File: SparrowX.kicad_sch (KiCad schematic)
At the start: 30 parts, among them J1 NORTH, J2 SOUTH, J3 WEST, J4 EAST, U1 LMR43610MSC3RPERQ1, U2 LD49100PU33RY, U3 STM32G0B1CBU6, U4 TCAN332G, U5 TCAN332G

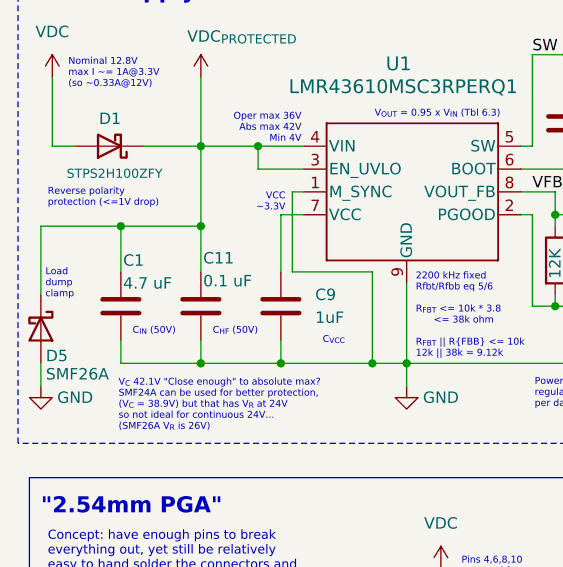
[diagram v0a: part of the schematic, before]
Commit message: DFM: get rid of 0201 SMD components
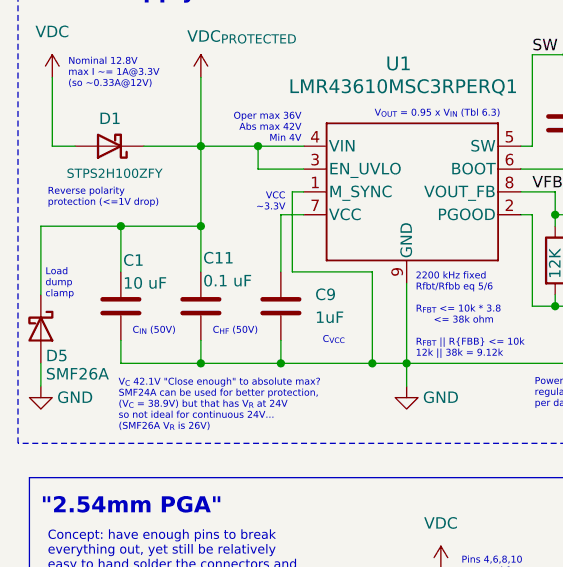
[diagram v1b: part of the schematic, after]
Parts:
- C1, C2: footprint Capacitor_SMD:C_0201_0603Metric -> Capacitor_SMD:C_0402_1005Metric
- C1: value 4.7 uF -> 10 uF
- R1: footprint Resistor_SMD:R_0201_0603Metric -> Resistor_SMD:R_0402_1005Metric
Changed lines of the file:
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@@
 			)
 		)
-		(property "Footprint" "Capacitor_SMD:C_0201_0603Metric"
+		(property "Footprint" "Capacitor_SMD:C_0402_1005Metric"
 			(at 106.68 70.8152 0)
 			(effects
@@
 			)
 		)
-		(property "Footprint" "Resistor_SMD:R_0201_0603Metric"
+		(property "Footprint" "Resistor_SMD:R_0402_1005Metric"
 			(at 98.552 85.09 90)
 			(effects
@@
 			)
 		)
-		(property "Value" "4.7 uF"
+		(property "Value" "10 uF"
 			(at 24.384 48.2599 0)
 			(effects
@@
 			)
 		)
-		(property "Footprint" "Capacitor_SMD:C_0201_0603Metric"
+		(property "Footprint" "Capacitor_SMD:C_0402_1005Metric"
 			(at 101.2952 106.68 0)
 			(effects

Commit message: A2 revision
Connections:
- net GND: now also J1.2 (Pin_2); no longer J3.1 (Pin_1)
- net SWCLK: now also J3.7 (Pin_7); no longer J3.8 (Pin_8)
- net SWDIO: now also J3.8 (Pin_8); no longer J3.7 (Pin_7)
- net VDC: no longer J1.2 (Pin_2)
- no-connect marks 11 -> 12
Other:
- note added: "PIN 1 is key pin"
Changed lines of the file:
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@@
 	)
 	(junction
-		(at 78.74 57.15)
+		(at 72.39 82.55)
 		(diameter 0)
 		(color 0 0 0 0)
 	)
 	(junction
-		(at 27.94 130.81)
+		(at 78.74 57.15)
 		(diameter 0)
 		(color 0 0 0 0)
@@
 	)
 	(no_connect
+		(at 30.48 107.95)
+	)
+	(no_connect
 		(at 74.93 97.79)
 	)
@@
 	(wire
 		(pts
-			(xy 27.94 107.95) (xy 30.48 107.95)
-		)
-		(stroke
-			(width 0)
-			(type default)
-		)
-	)
-	(wire
-		(pts
 			(xy 123.19 36.83) (xy 123.19 45.72)
 		)
@@
 	(wire
 		(pts
-			(xy 27.94 130.81) (xy 27.94 107.95)
-		)
-		(stroke
-			(width 0)
-			(type default)
-		)
-	)
-	(wire
-		(pts
 			(xy 176.53 102.87) (xy 190.5 102.87)
 		)
@@
 	(wire
 		(pts
+			(xy 59.69 82.55) (xy 72.39 82.55)
+		)
+		(stroke
+			(width 0)
+			(type default)
+		)
+	)
+	(wire
+		(pts
 			(xy 30.48 128.27) (xy 21.59 128.27)
 		)
@@
 	(wire
 		(pts
-			(xy 59.69 80.01) (xy 59.69 85.09)
-		)
-		(stroke
-			(width 0)
-			(type default)
-		)
-	)
-	(wire
-		(pts
 			(xy 176.53 87.63) (xy 190.5 87.63)
 		)
@@
 	(wire
 		(pts
+			(xy 59.69 85.09) (xy 59.69 82.55)
+		)
+		(stroke
+			(width 0)
+			(type default)
+		)
+	)
+	(wire
+		(pts
 			(xy 139.7 71.12) (xy 139.7 57.15)
 		)
@@
 		)
 	)
+	(text "PIN 1 is\nkey pin"
+		(exclude_from_sim no)
+		(at 31.242 106.426 0)
+		(effects
+			(font
+				(size 0.762 0.762)
+			)
+			(justify right bottom)
+		)
+	)
 	(text "R_{FBT}\n1%"
 		(exclude_from_sim no)
@@
 	(text "Pins 4,6,8,10\nreserved for\nfuture boards\nwith 4x CAN"
 		(exclude_from_sim no)
-		(at 61.976 83.312 0)
+		(at 61.976 81.788 0)
 		(effects
 			(font
@@
 	)
 	(label "SWDIO"
-		(at 21.59 115.57 0)
+		(at 52.07 115.57 180)
 		(fields_autoplaced yes)
 		(effects
@@
 				(size 1.27 1.27)
 			)
-			(justify left bottom)
+			(justify right bottom)
 		)
 	)
@@
 	)
 	(label "SWCLK"
-		(at 52.07 115.57 180)
+		(at 21.59 115.57 0)
 		(fields_autoplaced yes)
 		(effects
@@
 				(size 1.27 1.27)
 			)
-			(justify right bottom)
+			(justify left bottom)
 		)
 	)
@@
 					(unit 1)
 				)
-			)
-		)
-	)
-	(symbol
-		(lib_id "power:VDC")
-		(at 59.69 80.01 0)
-		(unit 1)
-		(exclude_from_sim no)
-		(in_bom yes)
-		(on_board yes)
-		(dnp no)
-		(property "Reference" "#PWR019"
-			(at 59.69 82.55 0)
-			(effects
-				(font
-					(size 1.27 1.27)
-				)
-				(hide yes)
-			)
-		)
-		(property "Value" "VDC"
-			(at 59.69 74.93 0)
-			(effects
-				(font
-					(size 1.27 1.27)
-				)
-			)
-		)
-		(property "Footprint" ""
-			(at 59.69 80.01 0)
-			(effects
-				(font
-					(size 1.27 1.27)
-				)
-				(hide yes)
-			)
-		)
-		(property "Datasheet" ""
-			(at 59.69 80.01 0)
-			(effects
-				(font
-					(size 1.27 1.27)
-				)
-				(hide yes)
-			)
-		)
-		(property "Description" ""
-			(at 59.69 80.01 0)
-			(effects
-				(font
-					(size 1.27 1.27)
-				)
-				(hide yes)
-			)
-		)
-		(pin "1"
-		)
-		(instances
-			(project "SparrowX"
-				(path "/c35a64e4-2c93-4785-901b-32ffcab28aed"
-					(reference "#PWR019")
-					(unit 1)
-				)

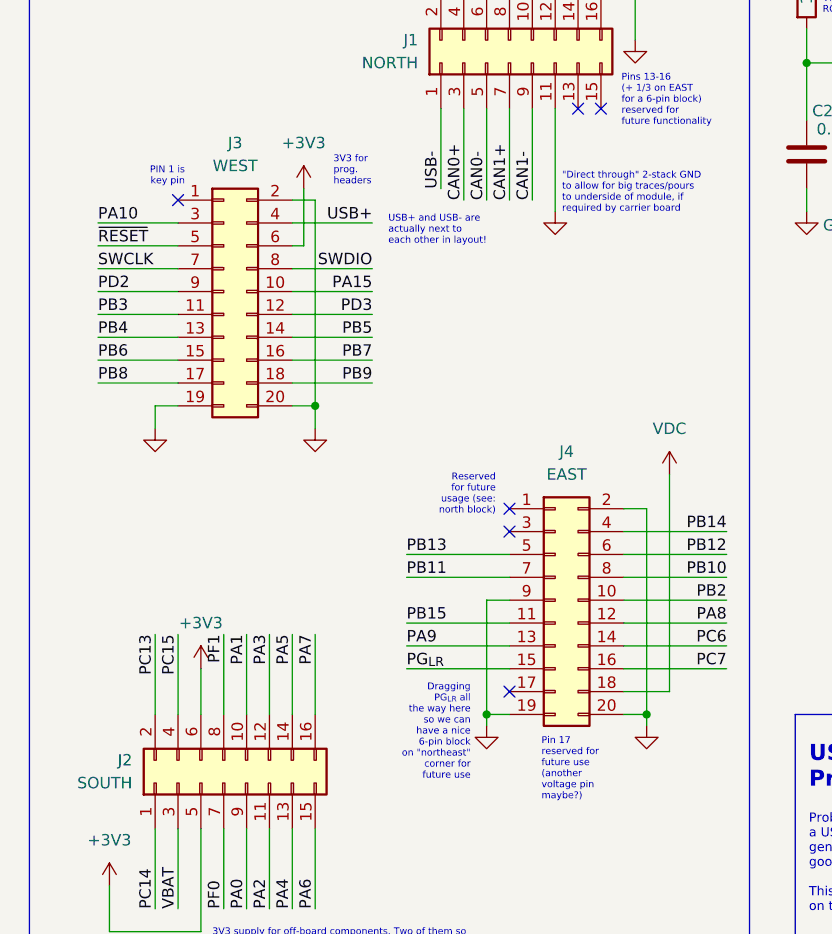
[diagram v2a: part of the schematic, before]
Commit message: Rev A2: add module corner key, silkscreen tweaks
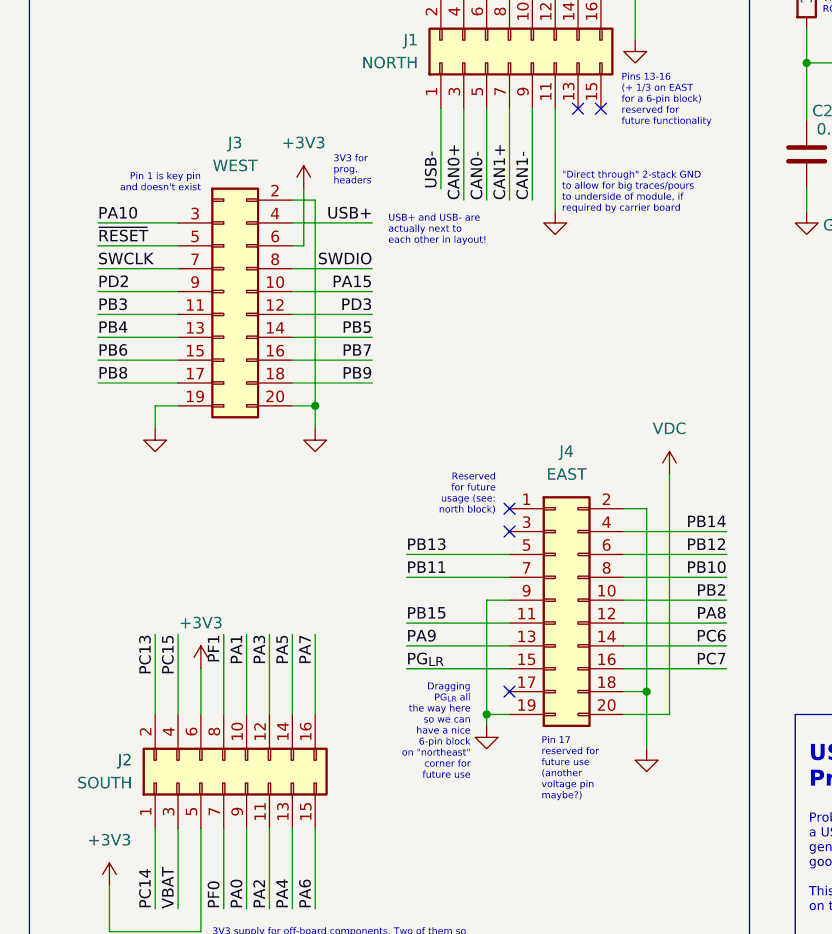
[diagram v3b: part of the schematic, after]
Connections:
- net GND: now also J4.18 (Pin_18); no longer J4.20 (Pin_20)
- net VDC: now also J4.20 (Pin_20); no longer J4.18 (Pin_18)
- no-connect marks 12 -> 11
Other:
- note added: "Pin 1 is key pin and doesn't exist"
- note removed: "PIN 1 is key pin"
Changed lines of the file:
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@@
 	)
 	(junction
-		(at 82.55 165.1)
+		(at 232.41 113.03)
 		(diameter 0)
 		(color 0 0 0 0)
 	)
 	(junction
-		(at 232.41 113.03)
+		(at 82.55 162.56)
 		(diameter 0)
 		(color 0 0 0 0)
@@
 	)
 	(no_connect
-		(at 30.48 107.95)
-	)
-	(no_connect
 		(at 74.93 97.79)
 	)
@@
 	(wire
 		(pts
-			(xy 85.09 138.43) (xy 85.09 162.56)
-		)
-		(stroke
-			(width 0)
-			(type default)
-		)
-	)
-	(wire
-		(pts
 			(xy 114.3 69.85) (xy 123.19 69.85)
 		)
@@
 	(wire
 		(pts
-			(xy 85.09 162.56) (xy 80.01 162.56)
+			(xy 85.09 165.1) (xy 80.01 165.1)
 		)
 		(stroke
@@
 	(wire
 		(pts
-			(xy 80.01 165.1) (xy 82.55 165.1)
+			(xy 152.4 121.92) (xy 152.4 135.89)
 		)
 		(stroke
@@
 	(wire
 		(pts
-			(xy 152.4 121.92) (xy 152.4 135.89)
+			(xy 91.44 160.02) (xy 80.01 160.02)
 		)
 		(stroke
@@
 	(wire
 		(pts
-			(xy 91.44 160.02) (xy 80.01 160.02)
+			(xy 149.86 121.92) (xy 149.86 135.89)
 		)
 		(stroke
@@
 	(wire
 		(pts
-			(xy 149.86 121.92) (xy 149.86 135.89)
+			(xy 33.02 33.02) (xy 39.37 33.02)
 		)
 		(stroke
@@
 	(wire
 		(pts
-			(xy 33.02 33.02) (xy 39.37 33.02)
+			(xy 33.02 57.15) (xy 41.91 57.15)
 		)
 		(stroke
@@
 	(wire
 		(pts
-			(xy 33.02 57.15) (xy 41.91 57.15)
+			(xy 232.41 49.53) (xy 232.41 58.42)
 		)
 		(stroke
@@
 	(wire
 		(pts
-			(xy 232.41 49.53) (xy 232.41 58.42)
+			(xy 100.33 106.68) (xy 100.33 109.22)
 		)
 		(stroke
@@
 	(wire
 		(pts
-			(xy 100.33 106.68) (xy 100.33 109.22)
+			(xy 80.01 162.56) (xy 82.55 162.56)
 		)
 		(stroke
@@
 	(wire
 		(pts
+			(xy 85.09 138.43) (xy 85.09 165.1)
+		)
+		(stroke
+			(width 0)
+			(type default)
+		)
+	)
+	(wire
+		(pts
 			(xy 30.48 165.1) (xy 30.48 156.21)
 		)
@@
 	(wire
 		(pts
+			(xy 82.55 162.56) (xy 82.55 168.91)
+		)
+		(stroke
+			(width 0)
+			(type default)
+		)
+	)
+	(wire
+		(pts
 			(xy 232.41 137.16) (xy 232.41 139.7)
 		)
@@
 	(wire
 		(pts
-			(xy 82.55 165.1) (xy 82.55 166.37)
+			(xy 82.55 142.24) (xy 82.55 162.56)
 		)
 		(stroke
@@
 	(wire
 		(pts
-			(xy 82.55 165.1) (xy 82.55 142.24)
-		)
-		(stroke
-			(width 0)
-			(type default)
-		)
-	)
-	(wire
-		(pts
 			(xy 30.48 123.19) (xy 21.59 123.19)
 		)
@@
 		)
 	)
-	(text "PIN 1 is\nkey pin"
+	(text "Pin 1 is key pin\nand doesn't exist"
 		(exclude_from_sim no)
-		(at 31.242 106.426 0)
+		(at 33.02 107.188 0)
 		(effects
 			(font
@@
 		(lib_name "GND_1")
 		(lib_id "power:GND")
-		(at 82.55 166.37 0)
+		(at 82.55 168.91 0)
 		(unit 1)
 		(exclude_from_sim no)
@@
 		(fields_autoplaced yes)
 		(property "Reference" "#PWR015"
-			(at 82.55 172.72 0)
+			(at 82.55 175.26 0)
 			(effects
 				(font
@@
 		)
 		(property "Value" "GND"
-			(at 82.55 171.45 0)
+			(at 82.55 173.99 0)
 			(effects
 				(font
@@
 		)
 		(property "Footprint" ""
-			(at 82.55 166.37 0)
+			(at 82.55 168.91 0)
 			(effects
 				(font
@@
 		)
 		(property "Datasheet" ""
-			(at 82.55 166.37 0)
+			(at 82.55 168.91 0)
 			(effects
 				(font
@@
 		)
 		(property "Description" "Power symbol creates a global label with name \"GND\" , ground"
-			(at 82.55 166.37 0)
+			(at 82.55 168.91 0)
 			(effects
 				(font
@@
 	)
 	(symbol
+		(lib_name "Conn_02x10_Odd_Even_1")
 		(lib_id "Connector_Generic:Conn_02x10_Odd_Even")
 		(at 35.56 118.11 0)
@@
 		(pin "14"
 		)
-		(pin "1"
-		)
 		(pin "5"
